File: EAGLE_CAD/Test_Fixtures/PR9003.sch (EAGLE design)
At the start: 20 parts

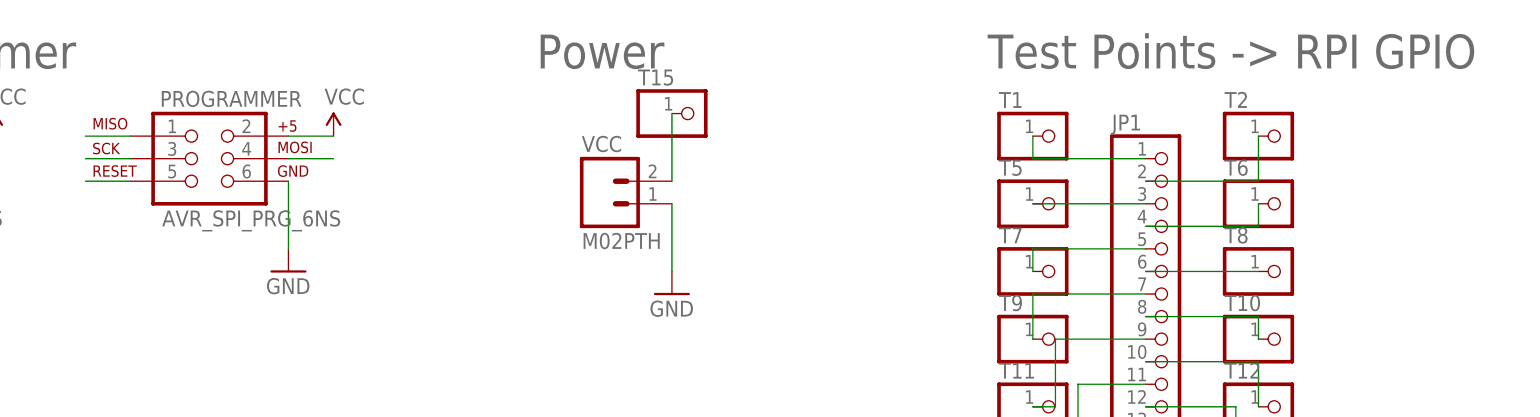
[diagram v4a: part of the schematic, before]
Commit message: PR9003 Updates
Updated masks
Added naming for GPIO breakout
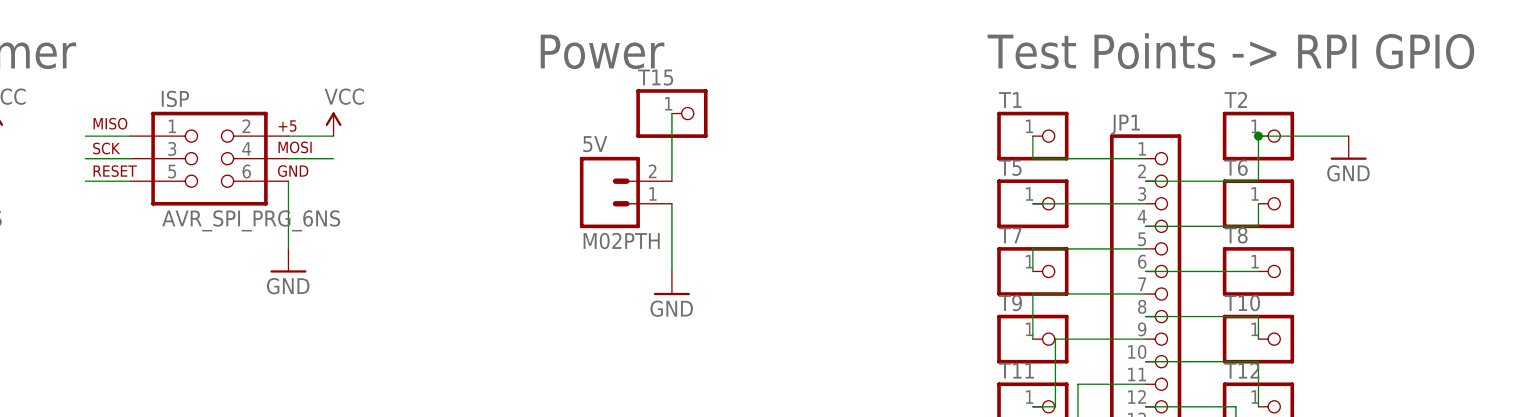
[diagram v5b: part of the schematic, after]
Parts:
- renumbered PROGRAMMER to ISP, VCC to 5V
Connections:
- removed net N$2: JP1.2, T2.1
- net GND: now also JP1.2, T2.1
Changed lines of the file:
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@@
 <parts>
 <part name="POGO" library="SparkFun-Connectors" deviceset="AVR_SPI_PRG_6" device="NS"/>
-<part name="PROGRAMMER" library="SparkFun-Connectors" deviceset="AVR_SPI_PRG_6" device="NS"/>
+<part name="ISP" library="SparkFun-Connectors" deviceset="AVR_SPI_PRG_6" device="NS"/>
 <part name="GND1" library="SparkFun-Aesthetics" deviceset="GND" device=""/>
 <part name="GND2" library="SparkFun-Aesthetics" deviceset="GND" device=""/>
 <part name="SUPPLY1" library="SparkFun-Aesthetics" deviceset="VCC" device=""/>
 <part name="SUPPLY2" library="SparkFun-Aesthetics" deviceset="VCC" device=""/>
-<part name="VCC" library="SparkFun-Connectors" deviceset="M02" device="PTH"/>
+<part name="5V" library="SparkFun-Connectors" deviceset="M02" device="PTH"/>
 <part name="GND3" library="SparkFun-Aesthetics" deviceset="GND" device=""/>
 <part name="T1" library="adafruit" deviceset="PINHD-1X1" device=""/>
@@
 <part name="U$1" library="PR_Parts_Library" deviceset="C&amp;K_D6C_SWITCH" device=""/>
 <part name="GND4" library="SparkFun-Aesthetics" deviceset="GND" device=""/>
+<part name="GND5" library="SparkFun-Aesthetics" deviceset="GND" device=""/>
 </parts>
 <sheets>
@@
 <instances>
 <instance part="POGO" gate="G$1" x="20.32" y="17.78"/>
-<instance part="PROGRAMMER" gate="G$1" x="58.42" y="17.78"/>
+<instance part="ISP" gate="G$1" x="58.42" y="17.78"/>
 <instance part="GND1" gate="1" x="30.48" y="5.08"/>
 <instance part="GND2" gate="1" x="68.58" y="5.08"/>
 <instance part="SUPPLY1" gate="G$1" x="35.56" y="20.32"/>
 <instance part="SUPPLY2" gate="G$1" x="73.66" y="20.32"/>
-<instance part="VCC" gate="G$1" x="104.14" y="12.7"/>
+<instance part="5V" gate="G$1" x="104.14" y="12.7"/>
 <instance part="GND3" gate="1" x="111.76" y="2.54"/>
 <instance part="T1" gate="G$1" x="154.94" y="20.32"/>
@@
 <instance part="U$1" gate="G$1" x="152.4" y="-45.72"/>
 <instance part="GND4" gate="1" x="144.78" y="-50.8"/>
+<instance part="GND5" gate="1" x="187.96" y="17.78"/>
 </instances>
 <busses>
@@
 </segment>
 <segment>
-<pinref part="PROGRAMMER" gate="G$1" pin="1"/>
+<pinref part="ISP" gate="G$1" pin="1"/>
 <wire x1="50.8" y1="20.32" x2="45.72" y2="20.32" width="0.1524" layer="91"/>
 </segment>
@@
 </segment>
 <segment>
-<pinref part="PROGRAMMER" gate="G$1" pin="3"/>
+<pinref part="ISP" gate="G$1" pin="3"/>
 <wire x1="50.8" y1="17.78" x2="45.72" y2="17.78" width="0.1524" layer="91"/>
 </segment>
@@
 </segment>
 <segment>
-<pinref part="PROGRAMMER" gate="G$1" pin="5"/>
+<pinref part="ISP" gate="G$1" pin="5"/>
 <wire x1="50.8" y1="15.24" x2="45.72" y2="15.24" width="0.1524" layer="91"/>
 </segment>
@@
 </segment>
 <segment>
-<pinref part="PROGRAMMER" gate="G$1" pin="4"/>
+<pinref part="ISP" gate="G$1" pin="4"/>
 <wire x1="68.58" y1="17.78" x2="73.66" y2="17.78" width="0.1524" layer="91"/>
 </segment>
@@
 </segment>
 <segment>
-<pinref part="PROGRAMMER" gate="G$1" pin="6"/>
+<pinref part="ISP" gate="G$1" pin="6"/>
 <wire x1="68.58" y1="15.24" x2="68.58" y2="7.62" width="0.1524" layer="91"/>
 <pinref part="GND2" gate="1" pin="GND"/>
 </segment>
 <segment>
-<pinref part="VCC" gate="G$1" pin="1"/>
+<pinref part="5V" gate="G$1" pin="1"/>
 <pinref part="GND3" gate="1" pin="GND"/>
 <wire x1="111.76" y1="5.08" x2="111.76" y2="12.7" width="0.1524" layer="91"/>
@@
 <pinref part="U$1" gate="G$1" pin="P$1"/>
 </segment>
+<segment>
+<pinref part="T2" gate="G$1" pin="1"/>
+<pinref part="GND5" gate="1" pin="GND"/>
+<wire x1="187.96" y1="20.32" x2="177.8" y2="20.32" width="0.1524" layer="91"/>
+<pinref part="JP1" gate="A" pin="2"/>
+<wire x1="165.1" y1="15.24" x2="177.8" y2="15.24" width="0.1524" layer="91"/>
+<wire x1="177.8" y1="15.24" x2="177.8" y2="20.32" width="0.1524" layer="91"/>
+<junction x="177.8" y="20.32"/>
+</segment>
 </net>
 <net name="VCC" class="0">
@@
 </segment>
 <segment>
-<pinref part="PROGRAMMER" gate="G$1" pin="2"/>
+<pinref part="ISP" gate="G$1" pin="2"/>
 <wire x1="68.58" y1="20.32" x2="73.66" y2="20.32" width="0.1524" layer="91"/>
 <pinref part="SUPPLY2" gate="G$1" pin="VCC"/>
@@
 <wire x1="165.1" y1="17.78" x2="152.4" y2="17.78" width="0.1524" layer="91"/>
 <wire x1="152.4" y1="17.78" x2="152.4" y2="20.32" width="0.1524" layer="91"/>
-</segment>
-</net>
-<net name="N$2" class="0">
-<segment>
-<pinref part="JP1" gate="A" pin="2"/>
-<wire x1="165.1" y1="15.24" x2="177.8" y2="15.24" width="0.1524" layer="91"/>
-<pinref part="T2" gate="G$1" pin="1"/>
-<wire x1="177.8" y1="15.24" x2="177.8" y2="20.32" width="0.1524" layer="91"/>
 </segment>
 </net>
@@
 <segment>
 <pinref part="T15" gate="G$1" pin="1"/>
-<pinref part="VCC" gate="G$1" pin="2"/>
+<pinref part="5V" gate="G$1" pin="2"/>
 <wire x1="111.76" y1="15.24" x2="111.76" y2="22.86" width="0.1524" layer="91"/>
 </segment>
